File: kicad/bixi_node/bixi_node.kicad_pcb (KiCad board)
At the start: 2 copper layers, 40.6 x 17.8 mm, 6 parts, among them CON1 BARREL_JACK, J1 RJ45, P1 CONN_01X03, U1 SP3485CN

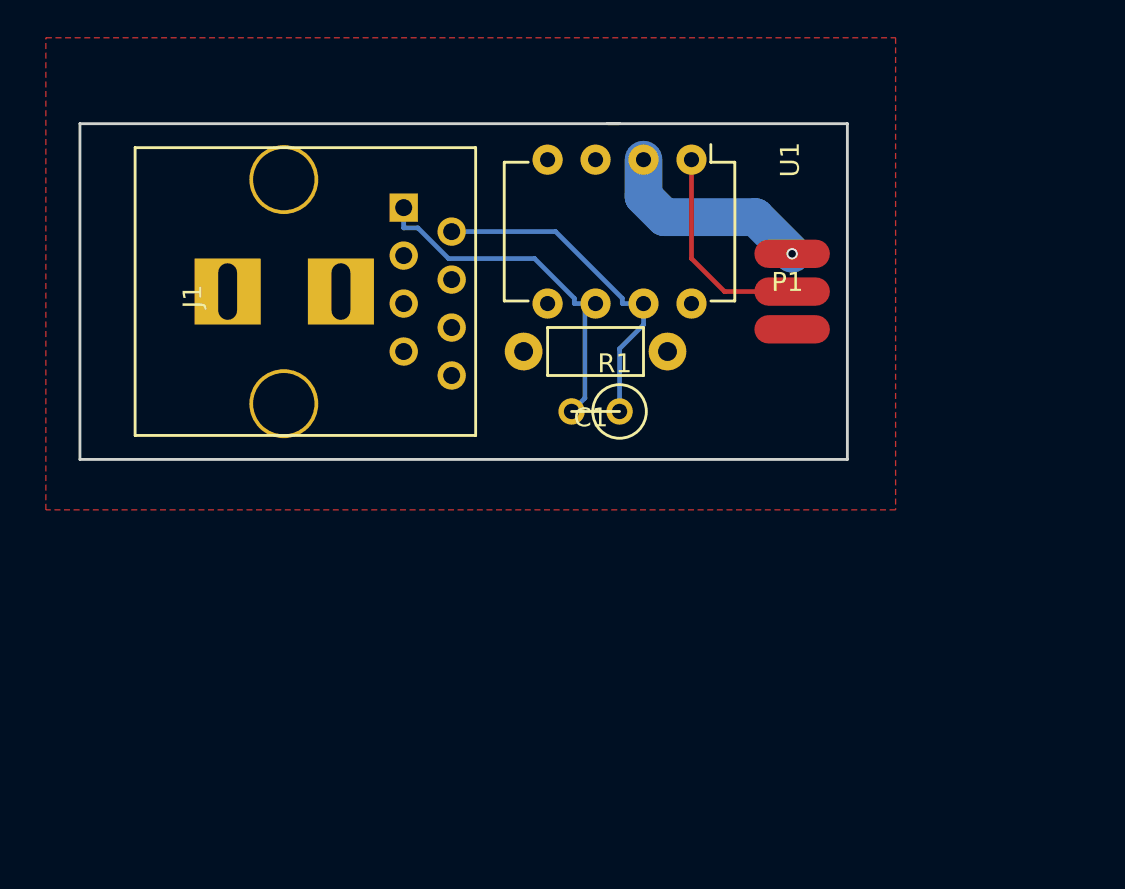
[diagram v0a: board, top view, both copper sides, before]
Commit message: controller board screw terminal, screw holes. ready for build
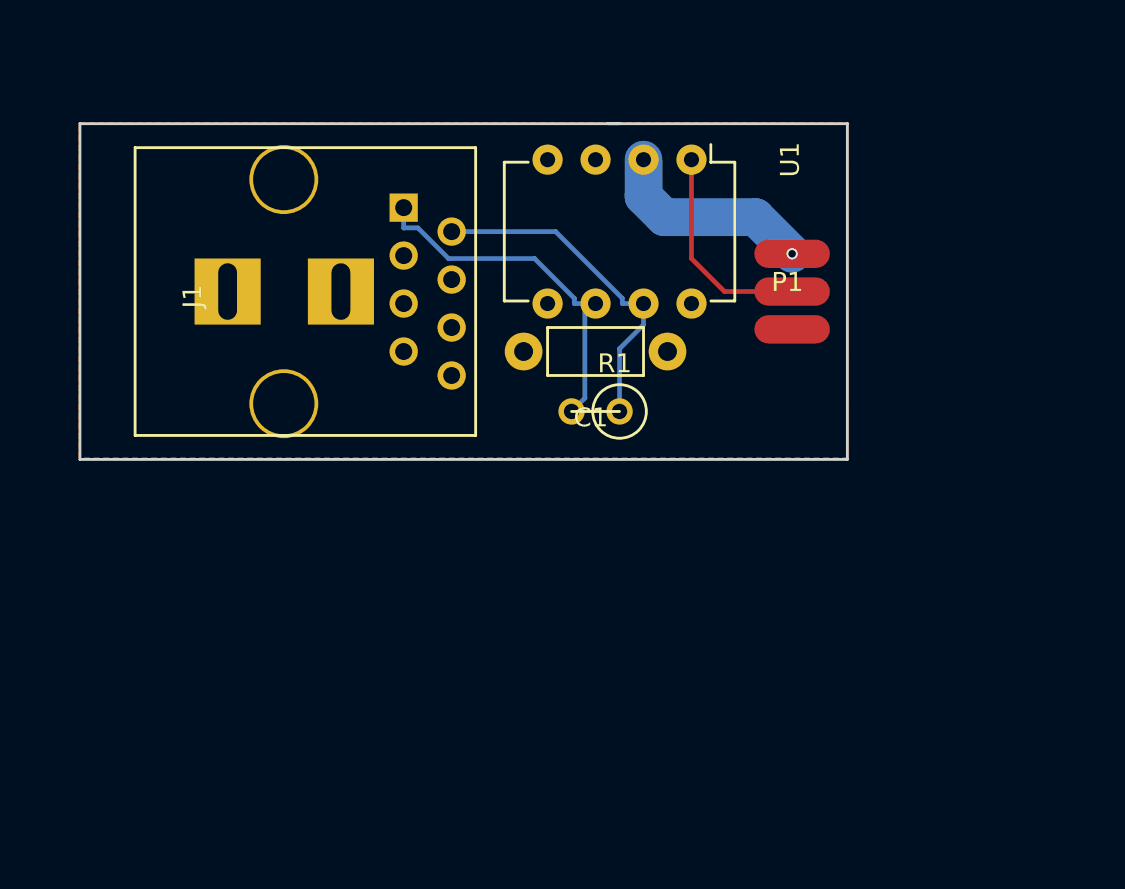
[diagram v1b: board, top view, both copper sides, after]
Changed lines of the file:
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@@
     (links 15)
     (no_connects 0)
-    (area 90.649379 80.350238 133.303334 100.405001)
+    (area 89 78 134.000001 103.000001)
     (thickness 1.6)
     (drawings 5)
@@
     (polygon
       (pts
-        (xy 134 103) (xy 89 103) (xy 89 78) (xy 134 78)
+        (xy 131.5 100.25) (xy 90.75 100.25) (xy 90.75 82.5) (xy 131.5 82.5)
       )
     )

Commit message: keep-out area for terminal block, finalized node pcb
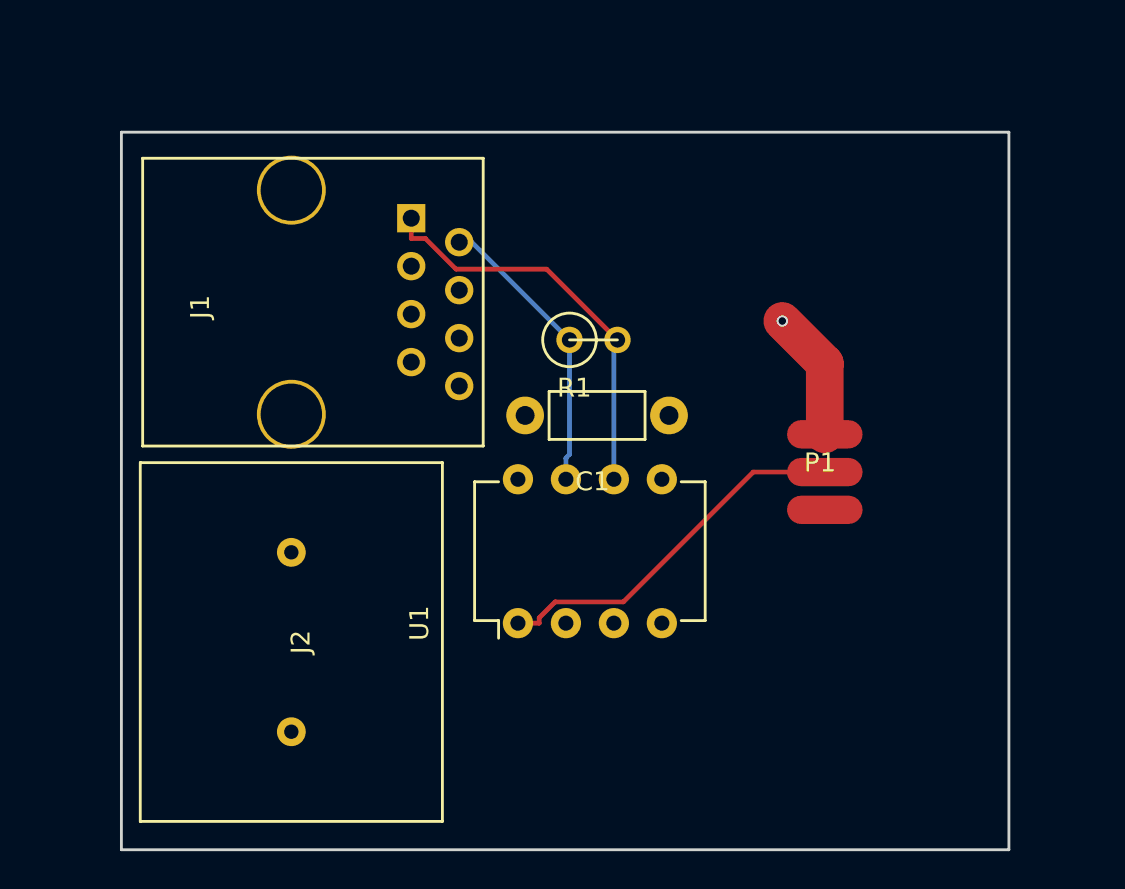
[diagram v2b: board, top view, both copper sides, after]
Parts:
- removed CON1: BARREL_JACK, custom:BARREL_JACK_2PIN
- added J2: Screw_Terminal_1x02, custom:HB9500-2P, F.Cu at (102.0, 110.0)
- moved U1 26.2 mm to (114.0, 109.0), turned to 90 degrees
- moved P1 9.72 mm to (130.0, 101.0)
- moved R1 3.79 mm to (118.0, 94.0), turned to 0 degrees
- moved C1 3.39 mm to (122.0, 98.0)
- moved J1 0.69 mm to (102.0, 92.0)
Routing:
- net Net-(P1-Pad2): track 11.3 -> 19.7 mm
- net GND: track 11.1 -> 6.93 mm
- net Net-(J1-Pad2): track 18.1 -> 15.4 mm
- net Net-(J1-Pad1): track 19.1 -> 21.7 mm
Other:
- board size 40.6 x 17.8 mm -> 47 x 38 mm
- net class Default: trace_width 0.25 -> 2

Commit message: larger pads on screw terminal connector
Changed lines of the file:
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@@
     (pcbplotparams
       (layerselection 0x00030_80000001)
-      (usegerberextensions false)
+      (usegerberextensions true)
       (excludeedgelayer true)
       (linewidth 0.100000)
@@
       (outputformat 1)
       (mirror false)
-      (drillshape 1)
+      (drillshape 0)
       (scaleselection 1)
       (outputdirectory ""))
@@
     (fp_line (start 9.5 8) (end -9.5 8) (layer F.SilkS) (width 0.15))
     (fp_line (start -9.5 8) (end -9.5 -8) (layer F.SilkS) (width 0.15))
-    (pad 1 thru_hole circle (at -4.75 0 90) (size 1.524 1.524) (drill 0.762) (layers *.Cu *.Mask)
-      (net 1 VCC))
-    (pad 2 thru_hole circle (at 4.75 0 90) (size 1.524 1.524) (drill 0.762) (layers *.Cu *.Mask)
-      (net 2 GND))
-  )
+    (pad 1 thru_hole circle (at -4.75 0 90) (size 2.6 2.6) (drill 1.3) (layers *.Cu *.Mask)
+      (net 1 VCC))
+    (pad 2 thru_hole circle (at 4.75 0 90) (size 2.6 2.6) (drill 1.3) (layers *.Cu *.Mask)
+      (net 2 GND))
+  )

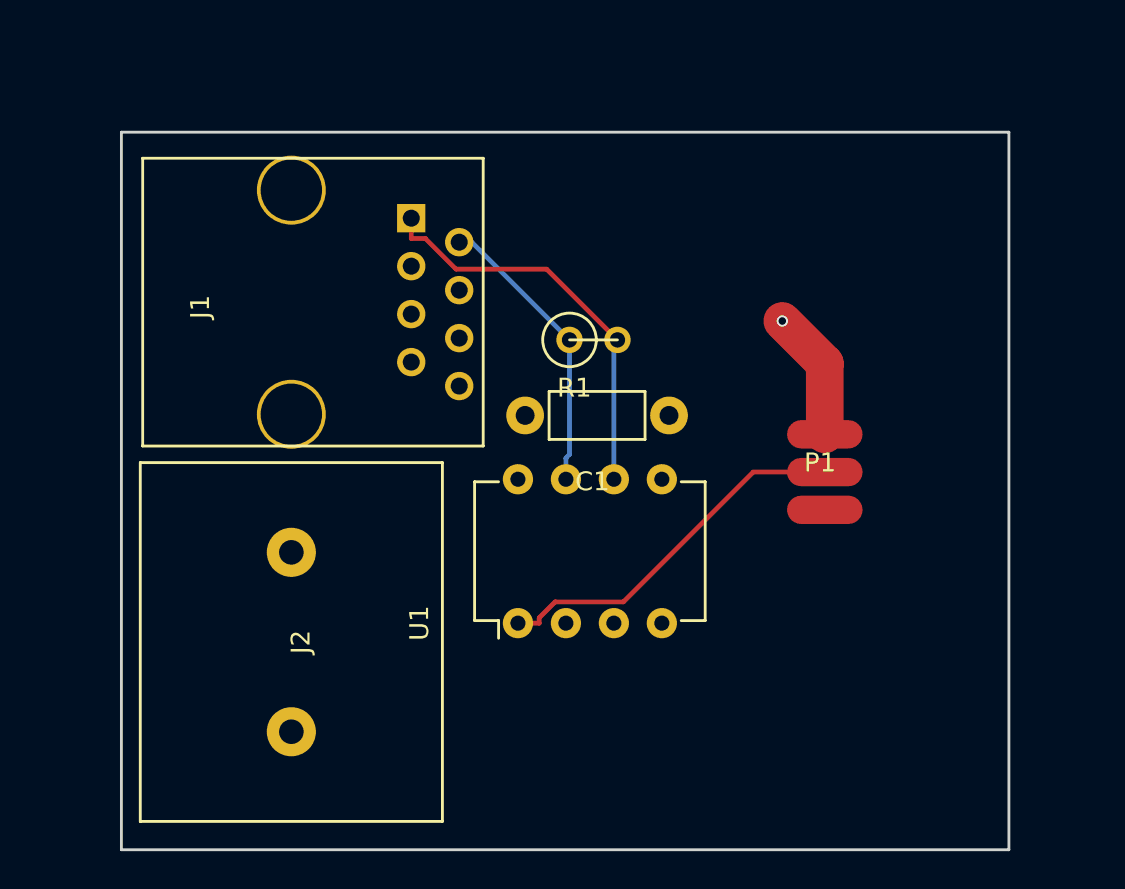
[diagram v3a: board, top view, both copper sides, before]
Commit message: both pcb's sent to fab
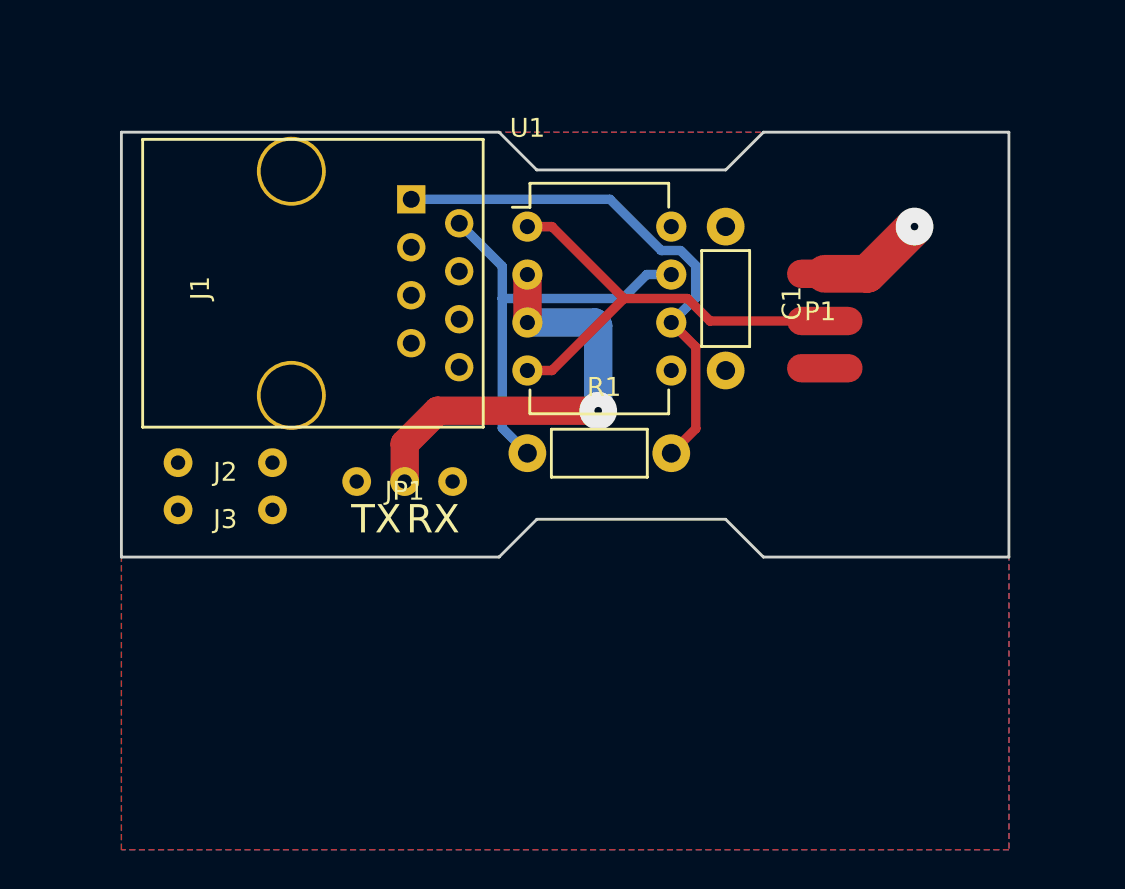
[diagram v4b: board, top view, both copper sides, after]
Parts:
- added J3: Screw_Terminal_1x01, custom:A116169CT_SPADE_CONNECTOR, F.Cu at (98.5, 103.0)
- added JP1: Jumper_NC_Dual, custom:jumper_3_pin_fixed, F.Cu at (108.0, 101.5)
- J2: value Screw_Terminal_1x02 -> Screw_Terminal_1x01; footprint custom:HB9500-2P -> custom:A116169CT_SPADE_CONNECTOR
- P1: footprint custom:PAD_3X_OVAL -> custom:PAD_3X_OVAL_WS2812B
- R1: footprint Discret:R1 -> Resistors_THT:Resistor_Horizontal_RM7mm
- moved U1 21.0 mm to (114.5, 88.0), turned to 0 degrees
- moved C1 10.4 mm to (125.0, 88.0), turned to 270 degrees
- moved J2 10.1 mm to (98.5, 100.5), turned to 0 degrees
- moved P1 8.00 mm to (130.0, 93.0)
- moved R1 6.95 mm to (114.5, 100.0)
- moved J1 1.00 mm to (102.0, 91.0)
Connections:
- J2 pad 2: GND -> (no net)
- P1 pad 2: Net-(P1-Pad2) -> /DATA
- U1 pad 1: Net-(P1-Pad2) -> /DATA
- U1 pad 2: GND -> Net-(JP1-Pad2)
- U1 pad 3: GND -> Net-(JP1-Pad2)
- U1 pad 4: Net-(U1-Pad4) -> /DATA
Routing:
- net /DATA: track 0.00 -> 24.5 mm
- net Net-(JP1-Pad2): track 0.00 -> 23.8 mm, vias 0 -> 1
- net Net-(P1-Pad2): track 19.7 -> 0.00 mm
- net Net-(J1-Pad2): track 15.4 -> 23.1 mm
- net Net-(J1-Pad1): track 21.7 -> 28.1 mm
- net GND: track 6.93 -> 5.79 mm
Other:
- board size 47 x 38 mm -> 47 x 22.5 mm
- net class Default: via_dia 0.6 -> 2
- board text added: "RX"
- board text added: "TX"

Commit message: v2 pcb
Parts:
- C1: footprint Resistors_THT:Resistor_Horizontal_RM7mm -> Capacitors_THT:C_Disc_D3.0mm_W2.0mm_P2.50mm
- moved J3 1.58 mm to (99.0, 104.5)
- moved J2 0.50 mm to (99.0, 100.5)
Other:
- board size 47 x 22.5 mm -> 47 x 24.5 mm
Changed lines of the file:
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@@
-(kicad_pcb (version 4) (host pcbnew 4.0.5)
+(kicad_pcb (version 4) (host pcbnew 4.0.6)
   (general
     (links 18)
     (no_connects 0)
-    (area 90.347618 81.805 140.075001 121.000001)
+    (area 90.847618 81.805 140.075001 121.000001)
     (thickness 1.6)
     (drawings 14)
@@
     (add_net VCC)
   )
-  (module Resistors_THT:Resistor_Horizontal_RM7mm (layer F.Cu)
-    (at 125 88 270)
-    (descr "Resistor, Axial,  RM 7.62mm, 1/3W,")
-    (tags "Resistor Axial RM 7.62mm 1/3W R3")
-    (fp_text reference C1 (at 4.05892 -3.50012 270) (layer F.SilkS)
-      (effects (font (size 1 1) (thickness 0.15)))
-    )
-    (fp_text value C (at 3.81 3.81 270) (layer F.Fab)
-      (effects (font (size 1 1) (thickness 0.15)))
-    )
-    (fp_line (start -1.25 -1.5) (end 8.85 -1.5) (layer F.CrtYd) (width 0.05))
-    (fp_line (start -1.25 1.5) (end -1.25 -1.5) (layer F.CrtYd) (width 0.05))
-    (fp_line (start 8.85 -1.5) (end 8.85 1.5) (layer F.CrtYd) (width 0.05))
-    (fp_line (start -1.25 1.5) (end 8.85 1.5) (layer F.CrtYd) (width 0.05))
-    (fp_line (start 1.27 -1.27) (end 6.35 -1.27) (layer F.SilkS) (width 0.15))
-    (fp_line (start 6.35 -1.27) (end 6.35 1.27) (layer F.SilkS) (width 0.15))
-    (fp_line (start 6.35 1.27) (end 1.27 1.27) (layer F.SilkS) (width 0.15))
-    (fp_line (start 1.27 1.27) (end 1.27 -1.27) (layer F.SilkS) (width 0.15))
-    (pad 1 thru_hole circle (at 0 0 270) (size 1.99898 1.99898) (drill 1.00076) (layers *.Cu *.SilkS *.Mask)
-      (net 1 VCC))
-    (pad 2 thru_hole circle (at 7.62 0 270) (size 1.99898 1.99898) (drill 1.00076) (layers *.Cu *.SilkS *.Mask)
-      (net 2 GND))
-  )
   (module Connectors:RJ45_8 (layer F.Cu)
     (at 102 91 270)
@@
     )
   )
-  (module custom:A116169CT_SPADE_CONNECTOR (layer F.Cu)
-    (at 98.5 100.5)
-    (fp_text reference J2 (at 0 0.5) (layer F.SilkS)
-      (effects (font (size 1 1) (thickness 0.15)))
-    )
-    (fp_text value Screw_Terminal_1x01 (at 0 -0.5) (layer F.Fab)
-      (effects (font (size 1 1) (thickness 0.15)))
-    )
-    (pad 1 thru_hole circle (at -2.5 0) (size 1.524 1.524) (drill 0.762) (layers *.Cu *.Mask)
-      (net 1 VCC))
-    (pad 2 thru_hole circle (at 2.5 0) (size 1.524 1.524) (drill 0.762) (layers *.Cu *.Mask))
-  )
-  (module custom:A116169CT_SPADE_CONNECTOR (layer F.Cu)
-    (at 98.5 103)
-    (fp_text reference J3 (at 0 0.5) (layer F.SilkS)
-      (effects (font (size 1 1) (thickness 0.15)))
-    )
-    (fp_text value Screw_Terminal_1x01 (at 0 -0.5) (layer F.Fab)
-      (effects (font (size 1 1) (thickness 0.15)))
-    )
-    (pad 1 thru_hole circle (at -2.5 0) (size 1.524 1.524) (drill 0.762) (layers *.Cu *.Mask)
-      (net 2 GND))
-    (pad 2 thru_hole circle (at 2.5 0) (size 1.524 1.524) (drill 0.762) (layers *.Cu *.Mask))
-  )
   (module Resistors_THT:Resistor_Horizontal_RM7mm (layer F.Cu)
     (at 114.5 100)
@@
       (net 9 /DATA))
   )
+  (module Capacitors_THT:C_Disc_D3.0mm_W2.0mm_P2.50mm (layer F.Cu)
+    (at 125 88 270)
+    (descr "C, Disc series, Radial, pin pitch=2.50mm, , diameter*width=3*2mm^2, Capacitor")
+    (tags "C Disc series Radial pin pitch 2.50mm  diameter 3mm width 2mm Capacitor")
+    (fp_text reference C1 (at 1.25 -2.06 270) (layer F.SilkS)
+      (effects (font (size 1 1) (thickness 0.15)))
+    )
+    (fp_text value C (at 1.25 2.06 270) (layer F.Fab)
+      (effects (font (size 1 1) (thickness 0.15)))
+    )
+    (fp_line (start -0.25 -1) (end -0.25 1) (layer F.Fab) (width 0.1))
+    (fp_line (start -0.25 1) (end 2.75 1) (layer F.Fab) (width 0.1))
+    (fp_line (start 2.75 1) (end 2.75 -1) (layer F.Fab) (width 0.1))
+    (fp_line (start 2.75 -1) (end -0.25 -1) (layer F.Fab) (width 0.1))
+    (fp_line (start -0.31 -1.06) (end 2.81 -1.06) (layer F.SilkS) (width 0.12))
+    (fp_line (start -0.31 1.06) (end 2.81 1.06) (layer F.SilkS) (width 0.12))
+    (fp_line (start -0.31 -1.06) (end -0.31 -0.996) (layer F.SilkS) (width 0.12))
+    (fp_line (start -0.31 0.996) (end -0.31 1.06) (layer F.SilkS) (width 0.12))
+    (fp_line (start 2.81 -1.06) (end 2.81 -0.996) (layer F.SilkS) (width 0.12))
+    (fp_line (start 2.81 0.996) (end 2.81 1.06) (layer F.SilkS) (width 0.12))
+    (fp_line (start -1.05 -1.35) (end -1.05 1.35) (layer F.CrtYd) (width 0.05))
+    (fp_line (start -1.05 1.35) (end 3.55 1.35) (layer F.CrtYd) (width 0.05))
+    (fp_line (start 3.55 1.35) (end 3.55 -1.35) (layer F.CrtYd) (width 0.05))
+    (fp_line (start 3.55 -1.35) (end -1.05 -1.35) (layer F.CrtYd) (width 0.05))
+    (pad 1 thru_hole circle (at 0 0 270) (size 1.6 1.6) (drill 0.8) (layers *.Cu *.Mask)
+      (net 1 VCC))
+    (pad 2 thru_hole circle (at 2.5 0 270) (size 1.6 1.6) (drill 0.8) (layers *.Cu *.Mask)
+      (net 2 GND))
+    (model Capacitors_THT.3dshapes/C_Disc_D3.0mm_W2.0mm_P2.50mm.wrl
+      (at (xyz 0 0 0))
+      (scale (xyz 0.393701 0.393701 0.393701))
+      (rotate (xyz 0 0 0))
+    )
+  )
+  (module custom:A116169CT_SPADE_CONNECTOR (layer F.Cu)
+    (at 99 100.5)
+    (fp_text reference J2 (at 0 0.5) (layer F.SilkS)
+      (effects (font (size 1 1) (thickness 0.15)))
+    )
+    (fp_text value Screw_Terminal_1x01 (at 0 -0.5) (layer F.Fab)
+      (effects (font (size 1 1) (thickness 0.15)))
+    )
+    (pad 1 thru_hole circle (at -2.5 0) (size 3 3) (drill 1.5) (layers *.Cu *.Mask)
+      (net 1 VCC))
+    (pad 2 thru_hole circle (at 2.5 0) (size 3 3) (drill 1.5) (layers *.Cu *.Mask))
+  )
+  (module custom:A116169CT_SPADE_CONNECTOR (layer F.Cu)
+    (at 99 104.5)
+    (fp_text reference J3 (at 0 0.5) (layer F.SilkS)
+      (effects (font (size 1 1) (thickness 0.15)))
+    )
+    (fp_text value Screw_Terminal_1x01 (at 0 -0.5) (layer F.Fab)
+      (effects (font (size 1 1) (thickness 0.15)))
+    )
+    (pad 1 thru_hole circle (at -2.5 0) (size 3 3) (drill 1.5) (layers *.Cu *.Mask)
+      (net 2 GND))
+    (pad 2 thru_hole circle (at 2.5 0) (size 3 3) (drill 1.5) (layers *.Cu *.Mask))
+  )
+  (gr_line (start 93 107.5) (end 93 83) (angle 90) (layer Edge.Cuts) (width 0.15))
+  (gr_line (start 140 83) (end 140 107.5) (angle 90) (layer Edge.Cuts) (width 0.15))
   (gr_text RX (at 109.5 103.5) (layer F.SilkS)
     (effects (font (size 1.5 1.5) (thickness 0.3)))
@@
     (effects (font (size 1.5 1.5) (thickness 0.3)))
   )
-  (gr_line (start 93 105.5) (end 93 83) (angle 90) (layer Edge.Cuts) (width 0.15))
-  (gr_line (start 140 83) (end 140 105.5) (angle 90) (layer Edge.Cuts) (width 0.15))
-  (gr_line (start 127 105.5) (end 140 105.5) (angle 90) (layer Edge.Cuts) (width 0.15))
-  (gr_line (start 125 103.5) (end 127 105.5) (angle 90) (layer Edge.Cuts) (width 0.15))
-  (gr_line (start 115 103.5) (end 125 103.5) (angle 90) (layer Edge.Cuts) (width 0.15))
-  (gr_line (start 113 105.5) (end 115 103.5) (angle 90) (layer Edge.Cuts) (width 0.15))
-  (gr_line (start 93 105.5) (end 113 105.5) (angle 90) (layer Edge.Cuts) (width 0.15))
+  (gr_line (start 127 107.5) (end 140 107.5) (angle 90) (layer Edge.Cuts) (width 0.15))
+  (gr_line (start 125 105.5) (end 127 107.5) (angle 90) (layer Edge.Cuts) (width 0.15))
+  (gr_line (start 115 105.5) (end 125 105.5) (angle 90) (layer Edge.Cuts) (width 0.15))
+  (gr_line (start 113 107.5) (end 115 105.5) (angle 90) (layer Edge.Cuts) (width 0.15))
+  (gr_line (start 93 107.5) (end 113 107.5) (angle 90) (layer Edge.Cuts) (width 0.15))
   (gr_line (start 127 83) (end 140 83) (angle 90) (layer Edge.Cuts) (width 0.15))
   (gr_line (start 125 85) (end 127 83) (angle 90) (layer Edge.Cuts) (width 0.15))
@@
   (gr_line (start 113 83) (end 115 85) (angle 90) (layer Edge.Cuts) (width 0.15))
   (gr_line (start 93 83) (end 113 83) (angle 90) (layer Edge.Cuts) (width 0.15))
-  (segment (start 130.25 90.5) (end 132.5 90.5) (width 2) (layer F.Cu) (net 2) (status 400000))
+  (segment (start 130.25 90.5) (end 132.5 90.5) (width 2) (layer F.Cu) (net 2))
   (via (at 135 88) (size 2) (drill 0.4) (layers F.Cu B.Cu) (net 2))
   (segment (start 132.5 90.5) (end 135 88) (width 2) (layer F.Cu) (net 2))

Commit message: bixi node updates
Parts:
- C1: footprint Capacitors_THT:C_Disc_D3.0mm_W2.0mm_P2.50mm -> Capacitors_THT:C_Axial_L3.8mm_D2.6mm_P7.50mm_Horizontal
- moved JP1 24.5 mm to (132.5, 102.0)
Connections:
- net Net-(J1-Pad1) renamed /DATA_DIFF_A
- net Net-(J1-Pad2) renamed /DATA_DIFF_B
- net Net-(JP1-Pad2) renamed /MODE
- J1 pad 3: Net-(J1-Pad3) -> /DATA
- J1 pad 5: Net-(J1-Pad5) -> VCC
- J1 pad 6: Net-(J1-Pad6) -> VCC
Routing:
- net /DATA: track 24.5 -> 35.5 mm
- net /DATA_DIFF_A: track 28.1 -> 25.2 mm
- net /DATA_DIFF_B: track 23.1 -> 24.4 mm
- net GND: track 5.79 -> 4.99 mm
- net /MODE: track 23.8 -> 24.2 mm, vias 1 -> 0
